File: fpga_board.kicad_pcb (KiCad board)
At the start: 8 copper layers, 50 x 50 mm, 142 parts, among them Q1 2N7002PW, Q2 2N7002PW, Q3 2N7002PW, Q4 2N7002PW, Q5 2N7002PW, Q6 2N7002PW, SW1 1TS028A-1300-0600-CT, U1 LFE5U-45F-7BG256I, U10 TLV62569DRL, U2 CYUSB3014-BZXC, U5 K4B4G1646E-BCMA, U6 K4B4G1646E-BCMA, U7 TLV62569DRL, U8 TLV62569DRL, U9 TLV62569DRL, X1 XO32, Y1 Crystal_GND24

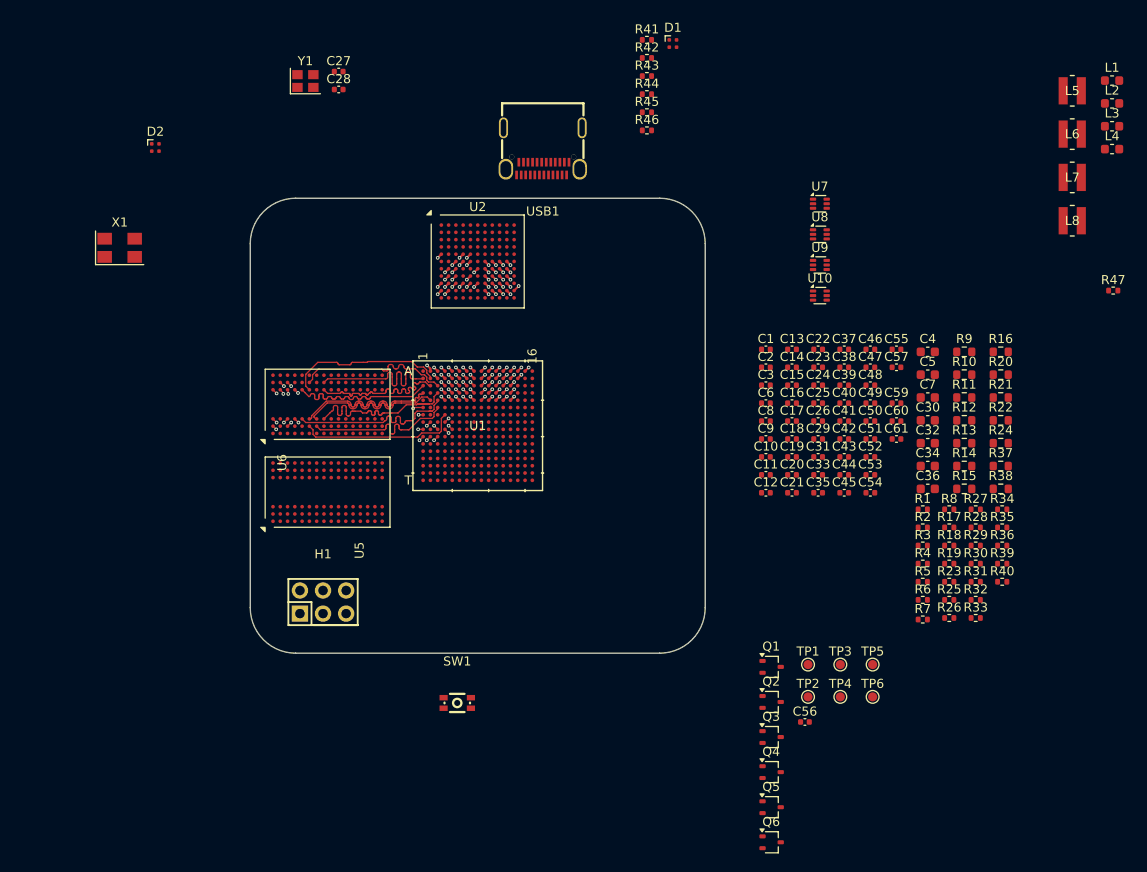
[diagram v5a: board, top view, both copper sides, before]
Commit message: added pre-commit for schematic svg generation, edited readme, organized schematic.
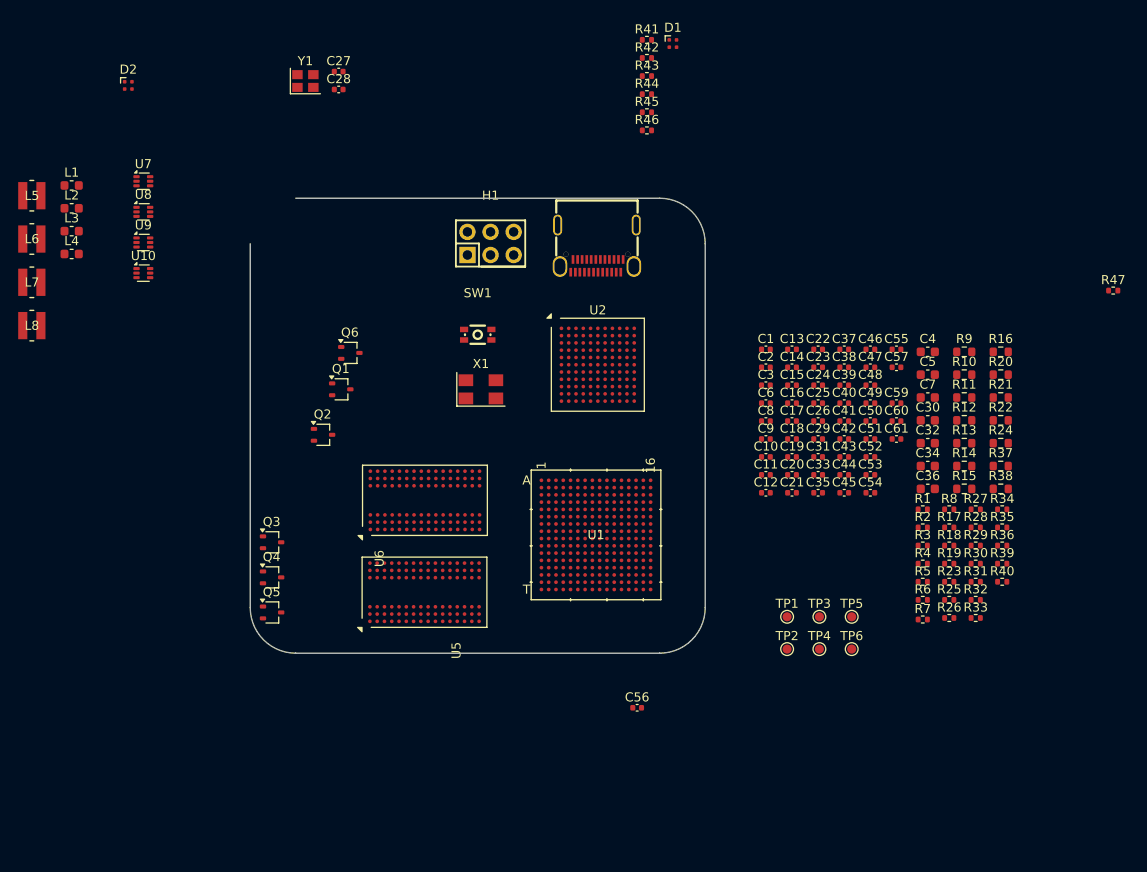
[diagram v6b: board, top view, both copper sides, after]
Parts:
- moved L1 114.9 mm to (50.4, 38.6)
- moved L2 114.9 mm to (50.4, 41.1)
- moved L3 114.9 mm to (50.4, 43.6)
- moved L4 114.9 mm to (50.4, 46.1)
- moved L5 114.9 mm to (46.0, 39.7)
- moved L6 114.9 mm to (46.0, 44.5)
- moved L7 114.9 mm to (46.0, 49.2)
- moved L8 114.9 mm to (46.0, 54.0)
- moved U10 74.4 mm to (58.2, 48.2)
- moved U7 74.4 mm to (58.2, 38.1)
- moved U8 74.4 mm to (58.2, 41.5)
- moved U9 74.4 mm to (58.2, 44.9)
- moved Q6 71.0 mm to (81.0, 57.0)
- moved Q3 58.9 mm to (72.4, 77.8)
- moved Q5 58.9 mm to (72.4, 85.5)
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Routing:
- net FIFO.FLAG_A: track 20.4 -> 0.00 mm, vias 2 -> 0
- net BYTE_LANE_0_4: track 20.4 -> 0.00 mm
- net BYTE_LANE_1_5: track 20.1 -> 0.00 mm, vias 2 -> 0
- net FIFO.SLCS#: track 20.0 -> 0.00 mm, vias 2 -> 0
- net BYTE_LANE_1_3: track 19.5 -> 0.00 mm, vias 2 -> 0
- net BYTE_LANE_1_0: track 19.4 -> 0.00 mm, vias 2 -> 0
- net BYTE_LANE_0_0: track 19.2 -> 0.00 mm
- net FIFO_DQ3: track 19.1 -> 0.00 mm, vias 2 -> 0
- net FIFO_DQ22: track 19.1 -> 0.00 mm, vias 2 -> 0
- net BYTE_LANE_1_2: track 19.1 -> 0.00 mm, vias 2 -> 0
- net BYTE_LANE_1_7: track 19.1 -> 0.00 mm, vias 2 -> 0
- net FIFO_DQ0: track 19.0 -> 0.00 mm, vias 2 -> 0
- net FIFO_DQ21: track 19.0 -> 0.00 mm, vias 2 -> 0
- net FIFO_DQ6: track 19.0 -> 0.00 mm, vias 2 -> 0
- net FIFO_DQ18: track 19.0 -> 0.00 mm, vias 2 -> 0
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- added copper zone on In6.Cu, net GND
- removed copper zone on In1.Cu, net GND
